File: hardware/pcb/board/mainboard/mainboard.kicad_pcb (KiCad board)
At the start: 6 copper layers, 65 x 50 mm, 130 parts, among them J1 Conn_Coaxial, J10 USB_C_Receptacle, J11 2908-05WB-MG, J2 BATTERY_Insta_360_Ace_Pro, J3 Conn_02x35_Odd_Even_MountingP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, J4 Conn_02x40_Odd_Even_MountingP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, J5 Conn_02x40_Odd_Even_MountingP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, J6 USB_C_Receptacle, J7 Conn_01x30, J8 Conn_01x30, J9 Conn_01x30, Q1 BSS138, Q2 DMN3008SFG, Q3 DMN3008SFG, U1 TPS7A20_SOT-23, U10 FT232RL, U11 TPS7A20_SOT-23, U12 AP33771C, U13 TXS0104E, U2 LSM6DS3TR, U3 NEO-M8N, U4 BQ25606, U5 BQ27441-G1, U6 SN74LVC1T45DBVR, U7 LIS2MDL, U8 SN74LVC1T45DBVR, U9 TPS61235P

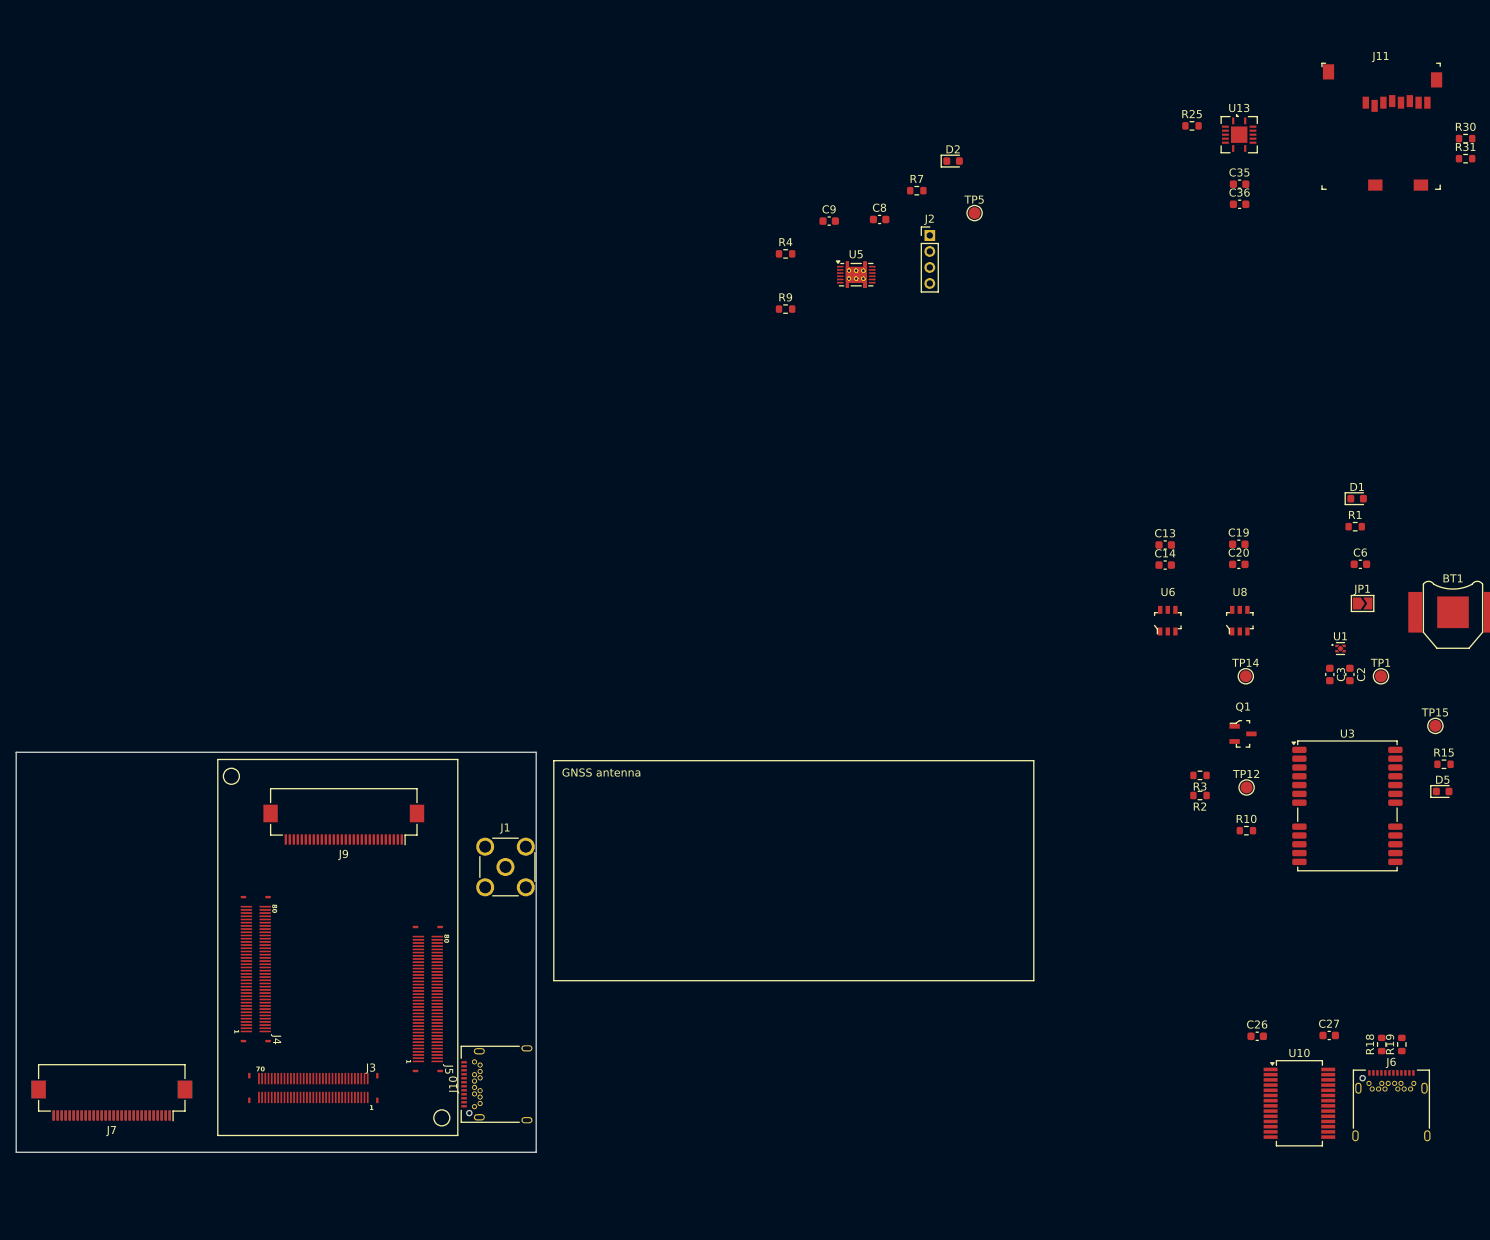
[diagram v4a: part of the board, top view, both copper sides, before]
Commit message: assign 3D models
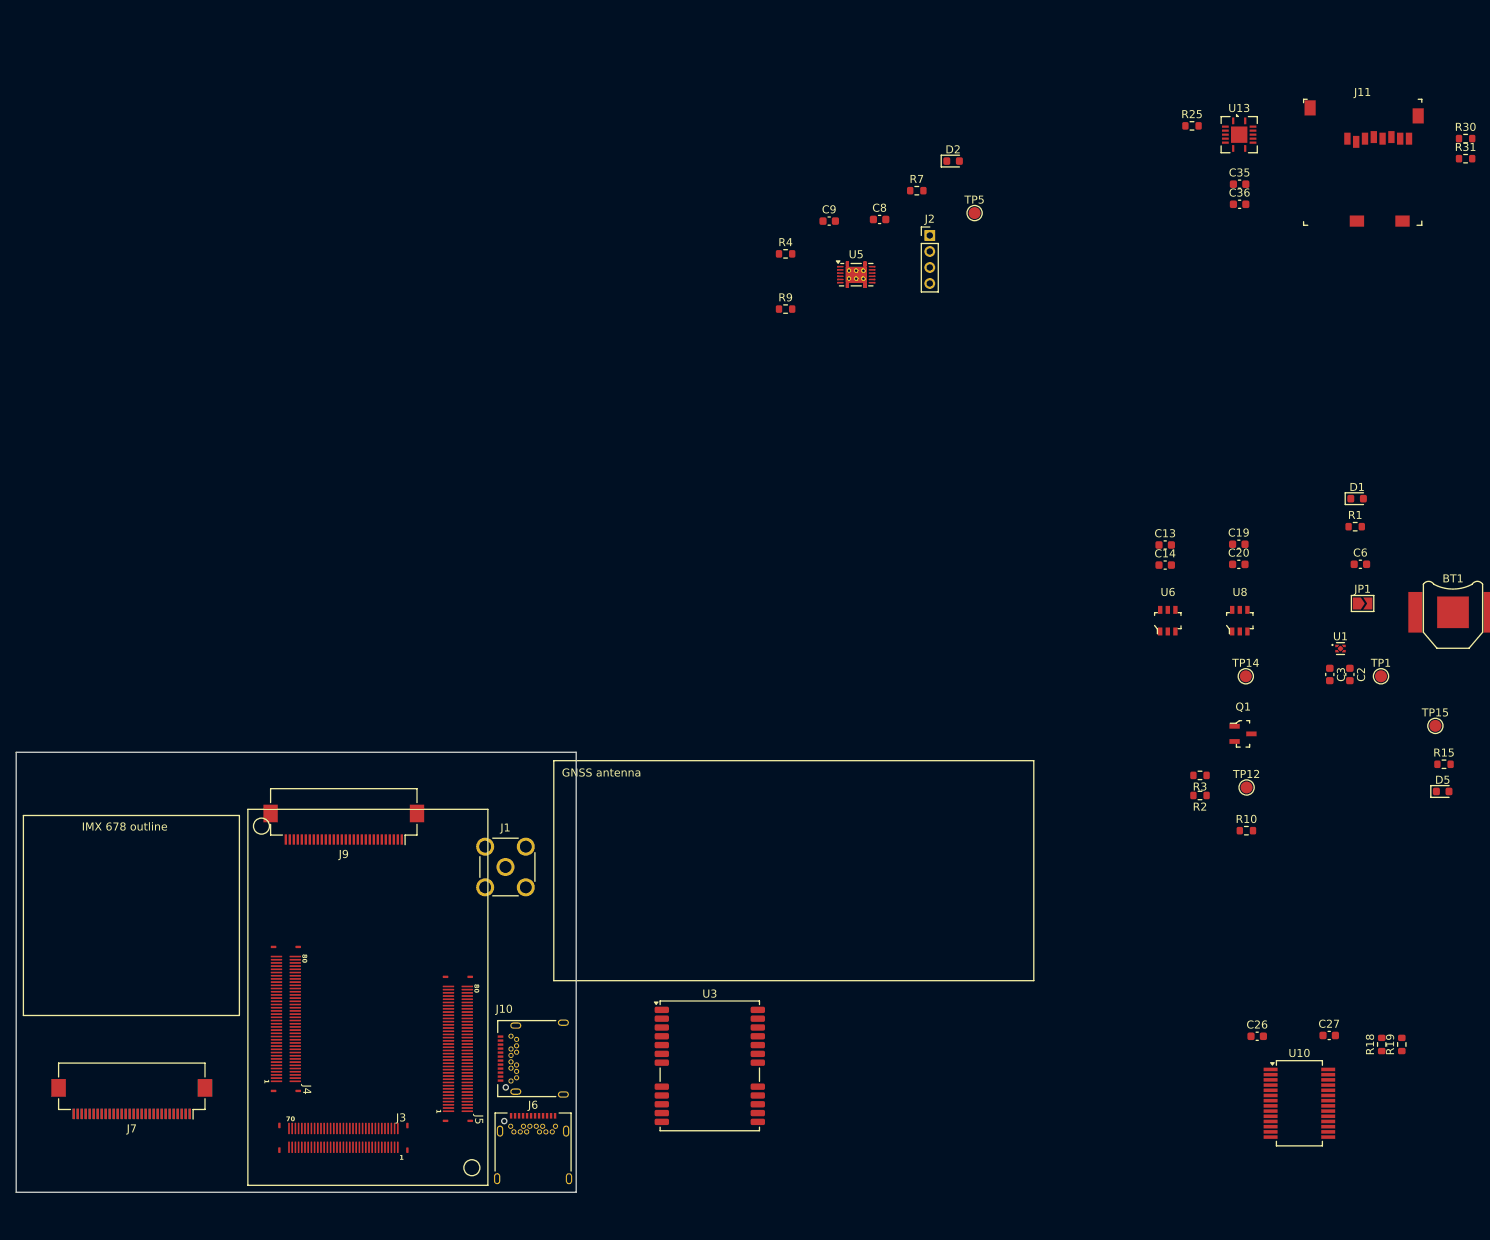
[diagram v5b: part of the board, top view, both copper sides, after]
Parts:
- moved J6 107.4 mm to (164.6, 150.5)
- moved U3 86.1 mm to (186.7, 139.2)
- moved J4 7.28 mm to (133.7, 133.3)
- moved J3 7.28 mm to (140.9, 148.2)
- moved J5 7.28 mm to (155.2, 137.1)
- moved J10 5.58 mm to (165.6, 138.3)
- moved J11 5.05 mm to (266.4, 23.3)
- moved J7 2.51 mm to (114.5, 143.3)
- moved J8 2.51 mm to (114.5, 143.3)
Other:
- board size 65 x 50 mm -> 70 x 55 mm
- board text added: "IMX 678 outline"
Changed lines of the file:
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@@
 		(tags "connector Hirose FH12 horizontal")
 		(property "Reference" "J9"
-			(at 0 -3.7 360)
+			(at 0 -3.7 0)
 			(layer "F.SilkS")
 			(effects
@@
 		)
 		(property "Value" "Conn_01x30"
-			(at 0 5.6 360)
+			(at 0 5.6 0)
 			(layer "F.Fab")
 			(effects
@@
 		)
 		(fp_text user "${REFERENCE}"
-			(at 0 3.7 360)
+			(at 0 3.7 0)
 			(layer "F.Fab")
 			(effects
@@
 		(tags "resistor")
 		(property "Reference" "R3"
-			(at 0 -1.43 360)
+			(at 0 -1.43 0)
 			(layer "F.SilkS")
 			(effects
@@
 		)
 		(property "Value" "0"
-			(at 0 1.43 360)
+			(at 0 1.43 0)
 			(layer "F.Fab")
 			(effects
@@
 		)
 		(fp_text user "${REFERENCE}"
-			(at 0 0 360)
+			(at 0 0 0)
 			(layer "F.Fab")
 			(effects
@@
 	(footprint "unsurv_offline_pcb_footprints:DF40_3.0_80"
 		(layer "F.Cu")
-		(at 129.95 127.1 -90)
+		(at 133.71 133.33 -90)
 		(property "Reference" "J4"
 			(at 8.83 -2.63 -90)
@@
 			(thermal_bridge_angle 45)
 		)
+		(model "${KICAD8_3DMODEL_DIR}/imported/DF40HC(3.0)-80DS.stp"
+			(offset
+				(xyz -5.9 0 1.5)
+			)
+			(scale
+				(xyz 1 1 1)
+			)
+			(rotate
+				(xyz -90 0 -90)
+			)
+		)
 	)
 	(footprint "LED_SMD:LED_0603_1608Metric"
@@
 		(tags "resistor")
 		(property "Reference" "R2"
-			(at 0 -1.43 360)
+			(at 0 -1.43 0)
 			(layer "F.SilkS")
 			(effects
@@
 		)
 		(property "Value" "0"
-			(at 0 1.43 360)
+			(at 0 1.43 0)
 			(layer "F.Fab")
 			(effects
@@
 		)
 		(fp_text user "${REFERENCE}"
-			(at 0 0 360)
+			(at 0 0 0)
 			(layer "F.Fab")
 			(effects
@@
 	(footprint "Connector_USB:USB_C_Receptacle_Amphenol_12401548E4-2A"
 		(layer "F.Cu")
-		(at 271.9 145.1)
+		(at 164.61 150.46)
 		(descr "USB TYPE C, RA RCPT PCB, Hybrid, https://www.amphenolcanada.com/StockAvailabilityPrice.aspx?From=&PartNum=12401548E4%7e2A")
 		(tags "USB C Type-C Receptacle Hybrid")
@@
 			)
 		)
+		(model "${KICAD8_3DMODEL_DIR}/Connector_USB.3dshapes/USB_C_Receptacle_Amphenol_12401610E4-2A.step"
+			(offset
+				(xyz 0 0 0)
+			)
+			(scale
+				(xyz 1 1 1)
+			)
+			(rotate
+				(xyz 0 0 0)
+			)
+		)
 	)
 	(footprint "Resistor_SMD:R_0603_1608Metric"
@@
 	(footprint "digikey-footprints:MicroSD_2908-05WB-MG"
 		(layer "F.Cu")
-		(at 268.7 18.8)
+		(at 266.4 23.3)
 		(property "Reference" "J11"
 			(at 1.9 -5.8 0)
@@
 			(pintype "passive")
 		)
+		(model "${KICAD8_3DMODEL_DIR}/imported/SD_card.STEP"
+			(offset
+				(xyz 2 -3 0)
+			)
+			(scale
+				(xyz 1 1 1)
+			)
+			(rotate
+				(xyz -90 0 0)
+			)
+		)
 	)
 	(footprint "Capacitor_SMD:C_0603_1608Metric"
@@
 	(footprint "unsurv_offline_pcb_footprints:DF40_3.0_70"
 		(layer "F.Cu")
-		(at 137.14 141.97)
+		(at 140.9 148.2)
 		(property "Reference" "J3"
 			(at 7.21 -2.52 0)
@@
 			(thermal_bridge_angle 45)
 		)
+		(model "${KICAD8_3DMODEL_DIR}/imported/DF40HC(3.0)-70DS.stp"
+			(offset
+				(xyz -4.9 0 1.5)
+			)
+			(scale
+				(xyz 1 1 1)
+			)
+			(rotate
+				(xyz -90 0 -90)
+			)
+		)
 	)
 	(footprint "TestPoint:TestPoint_Pad_D1.5mm"
@@
 	(footprint "unsurv_offline_pcb_footprints:DF40_3.0_80"
 		(layer "F.Cu")
-		(at 151.45 130.84 -90)
+		(at 155.21 137.07 -90)
 		(property "Reference" "J5"
 			(at 8.83 -2.63 -90)
@@
 			(thermal_bridge_angle 45)
 		)
+		(model "${KICAD8_3DMODEL_DIR}/imported/DF40HC(3.0)-80DS.stp"
+			(offset
+				(xyz -5.9 0 1.5)
+			)
+			(scale
+				(xyz 1 1 1)
+			)
+			(rotate
+				(xyz -90 0 -90)
+			)
+		)
 	)
 	(footprint "Capacitor_SMD:C_0603_1608Metric"
@@
 			(pintype "bidirectional")
 		)
+		(model "${KICAD8_3DMODEL_DIR}/Package_LGA.3dshapes/LGA-14_3x2.5mm_P0.5mm_LayoutBorder3x4y.step"
+			(offset
+				(xyz 0 0 0)
+			)
+			(scale
+				(xyz 1 1 1)
+			)
+			(rotate
+				(xyz 0 0 0)
+			)
+		)
 	)
 	(footprint "Battery:BatteryHolder_Keystone_2998_1x6.8mm"
@@
 			(pintype "passive")
 		)
-		(model "${KICAD8_3DMODEL_DIR}/Battery.3dshapes/BatteryHolder_Keystone_2998_1x6.8mm.wrl"
+		(model "${KICAD8_3DMODEL_DIR}/imported/2998--3DModel-STEP-630548.STEP"
 			(offset
-				(xyz 0 0 0)
+				(xyz 0 -3.5 2.9)
 			)
 			(scale
@@
 			)
 			(rotate
-				(xyz 0 0 0)
+				(xyz -90 0 0)
 			)
 		)
@@
 			)
 		)
+		(model "${KICAD8_3DMODEL_DIR}/Package_DFN_QFN.3dshapes/UDFN-4-1EP_1x1mm_P0.65mm_EP0.48x0.48mm.step"
+			(offset
+				(xyz 0 0 0)
+			)
+			(scale
+				(xyz 1 1 1)
+			)
+			(rotate
+				(xyz 0 0 0)
+			)
+		)
 	)
 	(footprint "RF_GPS:ublox_NEO"
 		(layer "F.Cu")
-		(at 266.4 106.7)
+		(at 186.7 139.2)
 		(descr "ublox NEO 6/7/8, (https://www.u-blox.com/sites/default/files/NEO-8Q-NEO-M8-FW3_HardwareIntegrationManual_%28UBX-15029985%29_0.pdf)")
 		(tags "GPS ublox NEO 6/7/8")
@@
 			(pintype "passive")
 		)
-		(model "${KICAD8_3DMODEL_DIR}/RF_GPS.3dshapes/ublox_NEO.wrl"
+		(model "${KICAD8_3DMODEL_DIR}/imported/NEO.STEP"
 			(offset
-				(xyz 0 0 0)
+				(xyz -47.5 18.1 0)
 			)
 			(scale
@@
 			)
 			(rotate
-				(xyz 0 0 0)
+				(xyz 0 0 180)
 			)
 		)
@@
 			)
 		)
+		(model "${KICAD8_3DMODEL_DIR}/Package_DFN_QFN.3dshapes/QFN-24-1EP_4x4mm_P0.5mm_EP2.6x2.6mm.step"
+			(offset
+				(xyz 0 0 0)
+			)
+			(scale
+				(xyz 1 1 1)
+			)
+			(rotate
+				(xyz 0 0 0)
+			)
+		)
 	)
 	(footprint "Capacitor_SMD:C_0603_1608Metric"
@@
 			(solder_paste_margin_ratio -0.00000001)
 		)
-		(model "${KICAD8_3DMODEL_DIR}/Package_SON.3dshapes/Texas_X2SON-4_1x1mm_P0.65mm.wrl"
+		(model "${KICAD8_3DMODEL_DIR}/Package_DFN_QFN.3dshapes/UDFN-4-1EP_1x1mm_P0.65mm_EP0.48x0.48mm.step"
 			(offset
 				(xyz 0 0 0)
@@
 	(footprint "Connector_USB:USB_C_Receptacle_Amphenol_12401548E4-2A"
 		(layer "F.Cu")
-		(at 161 141.5 90)
+		(at 165.56 138.29 90)
 		(descr "USB TYPE C, RA RCPT PCB, Hybrid, https://www.amphenolcanada.com/StockAvailabilityPrice.aspx?From=&PartNum=12401548E4%7e2A")
 		(tags "USB C Type-C Receptacle Hybrid")
 		(property "Reference" "J10"
-			(at 0 -6.36 90)
+			(at 6.19 -4.56 0)
 			(layer "F.SilkS")
 			(effects
@@
 			)
 		)
+		(model "${KICAD8_3DMODEL_DIR}/Connector_USB.3dshapes/USB_C_Receptacle_Amphenol_12401610E4-2A.step"
+			(offset
+				(xyz 0 0 0)
+			)
+			(scale
+				(xyz 1 1 1)
+			)
+			(rotate
+				(xyz 0 0 0)
+			)
+		)
 	)
 	(footprint "LED_SMD:LED_0603_1608Metric"
@@
 	(footprint "Connector_FFC-FPC:Hirose_FH12-30S-0.5SH_1x30-1MP_P0.50mm_Horizontal"
 		(layer "F.Cu")
-		(at 111.95 143.55 180)
+		(at 114.45 143.35 180)
 		(descr "Hirose FH12, FFC/FPC connector, FH12-30S-0.5SH, 30 Pins per row (https://www.hirose.com/product/en/products/FH12/FH12-24S-0.5SH(55)/), generated with kicad-footprint-generator")
 		(tags "connector Hirose FH12 horizontal")
 		(property "Reference" "J7"
-			(at 0 -3.7 360)
+			(at 0 -3.7 0)
 			(layer "F.SilkS")
 			(effects
@@
 		)
 		(property "Value" "Conn_01x30"
-			(at 0 5.6 360)
+			(at 0 5.6 0)
 			(layer "F.Fab")
 			(effects
@@
 		)
 		(fp_text user "${REFERENCE}"
-			(at 0 3.7 360)
+			(at 0 3.7 0)
 			(layer "F.Fab")
 			(effects
@@
 	(footprint "Connector_FFC-FPC:Hirose_FH12-30S-0.5SH_1x30-1MP_P0.50mm_Horizontal"
 		(layer "B.Cu")
-		(at 111.95 143.55)
+		(at 114.45 143.35)
 		(descr "Hirose FH12, FFC/FPC connector, FH12-30S-0.5SH, 30 Pins per row (https://www.hirose.com/product/en/products/FH12/FH12-24S-0.5SH(55)/), generated with kicad-footprint-generator")
 		(tags "connector Hirose FH12 horizontal")
 		(property "Reference" "J8"
-			(at 0 3.7 360)
+			(at 0 3.7 0)
 			(layer "B.SilkS")
 			(effects
@@
 		)
 		(property "Value" "Conn_01x30"
-			(at 0 -5.6 360)
+			(at 0 -5.6 0)
 			(layer "B.Fab")
 			(effects
@@
 		)
 		(fp_text user "${REFERENCE}"
-			(at 0 -3.7 360)
+			(at 0 -3.7 0)
 			(layer "B.Fab")
 			(effects
@@
 	)
 	(gr_rect
-		(start 125.2 100.9)
-		(end 155.2 147.9)
+		(start 128.96 107.13)
+		(end 158.96 154.13)
 		(stroke
 			(width 0.1)
@@
 	)
 	(gr_circle
-		(center 153.2 145.7)
-		(end 153.2 146.7)
+		(center 156.96 151.93)
+		(end 156.96 152.93)
+		(stroke
+			(width 0.1)
+			(type default)
+		)
+		(fill none)
+		(layer "F.SilkS")
+	)
+	(gr_rect
+		(start 100.9 107.9)
+		(end 127.9 132.9)
 		(stroke
 			(width 0.1)
@@
 	)
 	(gr_circle
-		(center 126.9 103)
-		(end 126.9 104)
+		(center 130.66 109.23)
+		(end 130.66 110.23)
 		(stroke
 			(width 0.1)
@@
 	(gr_rect
 		(start 100 100)
-		(end 165 150)
+		(end 170 155)
 		(stroke
 			(width 0.05)
@@
 		(layer "Edge.Cuts")
 	)
+	(gr_text "IMX 678 outline"
+		(at 108.2 109.9 0)
+		(layer "F.SilkS")
+		(effects
+			(font
+				(size 1 1)
+				(thickness 0.1)
+			)
+			(justify left bottom)
+		)
+	)
 	(gr_text "GNSS antenna"

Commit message: parts placement
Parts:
- removed TP1: TestPoint, TestPoint:TestPoint_Pad_D1.5mm
- added C38: 100 nF, Capacitor_SMD:C_0603_1608Metric, F.Cu at (337.2, 9.80)
- added D8: LED, LED_SMD:LED_0603_1608Metric, F.Cu at (333.7, 29.0)
- added R32: 100k, Resistor_SMD:R_0603_1608Metric, F.Cu at (336.9, 29.0)
- C26, C27, C35, C36, C37, C8, C9, D2, J11, J2, R18, R19, R25, R30, R31, R4, R7, R9, TP5, U10, U13, U5: moved to B.Cu
- J1: footprint Connector_Coaxial:SMA_Molex_73251-2200_Horizontal -> Connector_Coaxial:MMCX_Molex_73415-0961_Horizontal_1.6mm-PCB
- J10, J6: footprint Connector_USB:USB_C_Receptacle_Amphenol_12401548E4-2A -> Connector_USB:USB_C_CONN_1054550101_MOL
- moved C37 201.4 mm to (119.0, 131.4), turned to 180 degrees
- moved R30 196.7 mm to (119.0, 134.5), turned to 180 degrees
- moved R31 196.7 mm to (119.0, 137.0), turned to 180 degrees
- moved J11 191.9 mm to (105.4, 127.7), turned to -90 degrees
- moved U13 167.9 mm to (119.9, 125.3), turned to -90 degrees
- moved C35 162.3 mm to (118.9, 120.5), turned to -90 degrees
- moved C36 158.8 mm to (121.4, 120.5), turned to -90 degrees
- moved R25 157.6 mm to (124.1, 120.4), turned to -90 degrees
- moved BT1 141.0 mm to (140.5, 105.6)
- moved TP15 131.0 mm to (149.2, 123.8)
- moved JP1 129.4 mm to (142.6, 112.2)
- moved D1 128.1 mm to (147.0, 111.3)
- moved R1 127.2 mm to (147.0, 112.9), turned to 180 degrees
- moved C6 126.9 mm to (147.0, 114.5), turned to 180 degrees
- moved D2 126.1 mm to (150.6, 133.2), turned to 180 degrees
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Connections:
- C6 pad 1: Net-(BT1-+) -> V_BCKP
- R1 pad 1: Net-(BT1-+) -> V_BCKP
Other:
- board size 70 x 55 mm -> 72.5 x 55 mm
- board text added: "BATTERY"
- board text added: "FPC conn"

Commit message: parts placement
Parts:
- D6, D7, D8, R21, R27, R32: moved to B.Cu
- moved Q2 220.5 mm to (156.9, 142.2)
- moved Q3 220.5 mm to (156.9, 146.7)
- moved R20 220.1 mm to (158.4, 137.6), turned to 180 degrees
- moved R23 219.8 mm to (153.3, 143.1)
- moved C28 219.6 mm to (156.0, 136.8), turned to 90 degrees
- moved C34 219.6 mm to (157.4, 151.4)
- moved C33 219.6 mm to (157.4, 149.8)
- moved R22 219.5 mm to (154.2, 149.8)
- moved C38 218.9 mm to (158.4, 136.0), turned to 180 degrees
- moved U12 217.5 mm to (152.7, 146.6)
- moved R29 214.4 mm to (149.1, 148.2)
- moved R28 212.5 mm to (149.1, 146.6)
- moved C32 210.2 mm to (160.7, 136.8), turned to 90 degrees
- moved C31 209.9 mm to (162.3, 136.8), turned to 90 degrees
- moved R24 200.8 mm to (162.0, 142.6)
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
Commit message: preliminary placement of all parts
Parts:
- C21, C22, C23, C24, C25, D3, D4, L2, R12, R8, TP13, TP8, U9: moved to B.Cu
- R18, R19: moved to F.Cu
- moved TP13 260.5 mm to (142.2, 148.1), turned to 180 degrees
- moved C22 258.5 mm to (142.2, 151.2)
- moved C21 258.5 mm to (140.6, 151.2)
- moved C23 254.0 mm to (143.8, 151.2)
- moved U9 247.4 mm to (147.3, 151.4), turned to 180 degrees
- moved C11 242.2 mm to (147.3, 142.9), turned to -90 degrees
- moved C25 241.0 mm to (151.6, 153.3), turned to 180 degrees
- moved TP3 239.7 mm to (150.2, 138.8)
- moved L2 238.9 mm to (151.6, 151.7), turned to 180 degrees
- moved R12 238.2 mm to (137.1, 101.4), turned to 180 degrees
- moved R17 237.5 mm to (143.1, 147.2), turned to -90 degrees
- moved C24 236.8 mm to (151.6, 150.1), turned to 180 degrees
- moved D3 236.5 mm to (133.8, 101.4)
- moved C4 234.7 mm to (143.7, 137.7), turned to 90 degrees
- moved L1 233.5 mm to (145.3, 137.7), turned to 90 degrees
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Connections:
- U4 pad 22: unconnected-(U4-REGN-Pad22) -> REGN
